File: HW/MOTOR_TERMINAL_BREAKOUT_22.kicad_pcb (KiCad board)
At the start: 2 copper layers, 20 x 28 mm, 12 parts

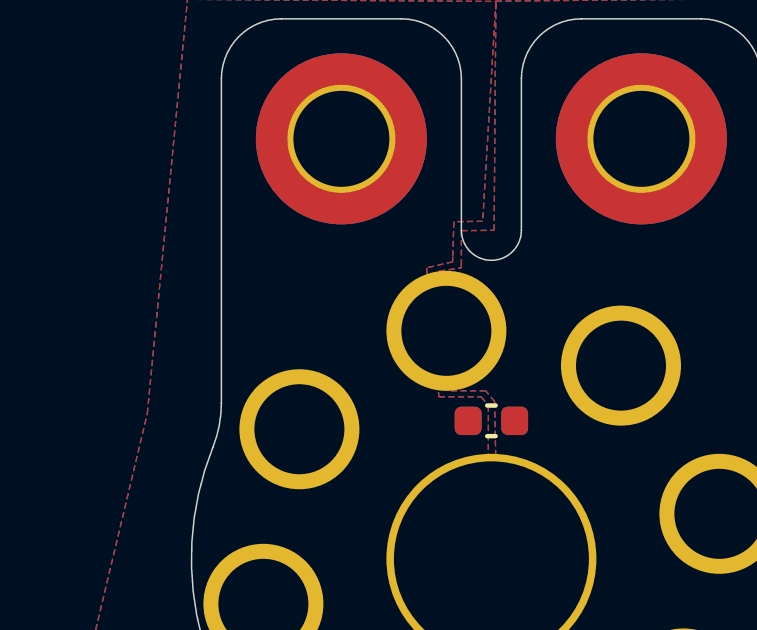
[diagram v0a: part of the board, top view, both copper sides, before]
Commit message: Update Silkscreen to Add Revision Number
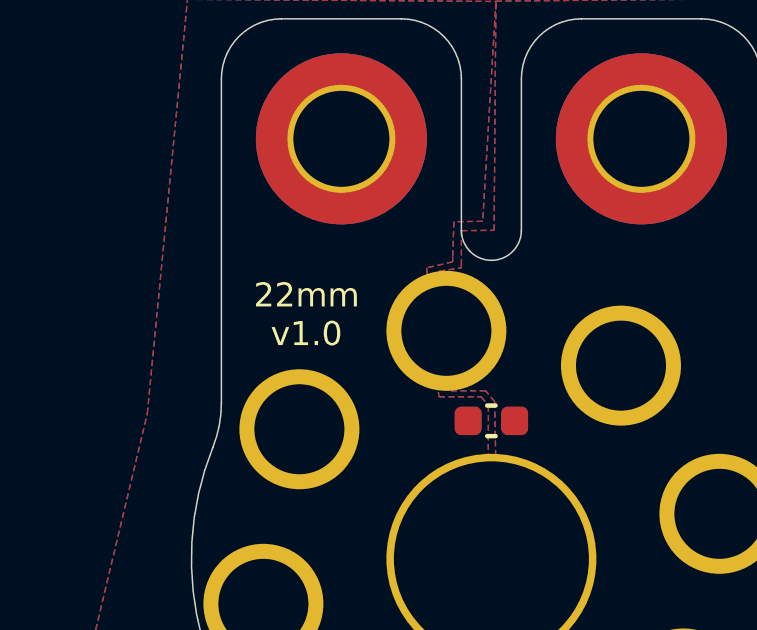
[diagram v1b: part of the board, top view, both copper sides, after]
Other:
- board text added: "22mm v1.0"
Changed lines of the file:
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@@
   (gr_line (start 221 134) (end 221 139.050126) (layer "Edge.Cuts") (width 0.05))
   (gr_arc (start 221 134) (mid 221.585786 132.585786) (end 223 132) (layer "Edge.Cuts") (width 0.05))
+  (gr_text "22mm\nv1.0" (at 213.84 141.86) (layer "F.SilkS")
+    (effects (font (size 0.8 0.8) (thickness 0.2)))
+  )
   (zone (net 2) (net_name "+BATT") (layers F&B.Cu) (hatch edge 0.508)
     (connect_pads yes (clearance 0.2))

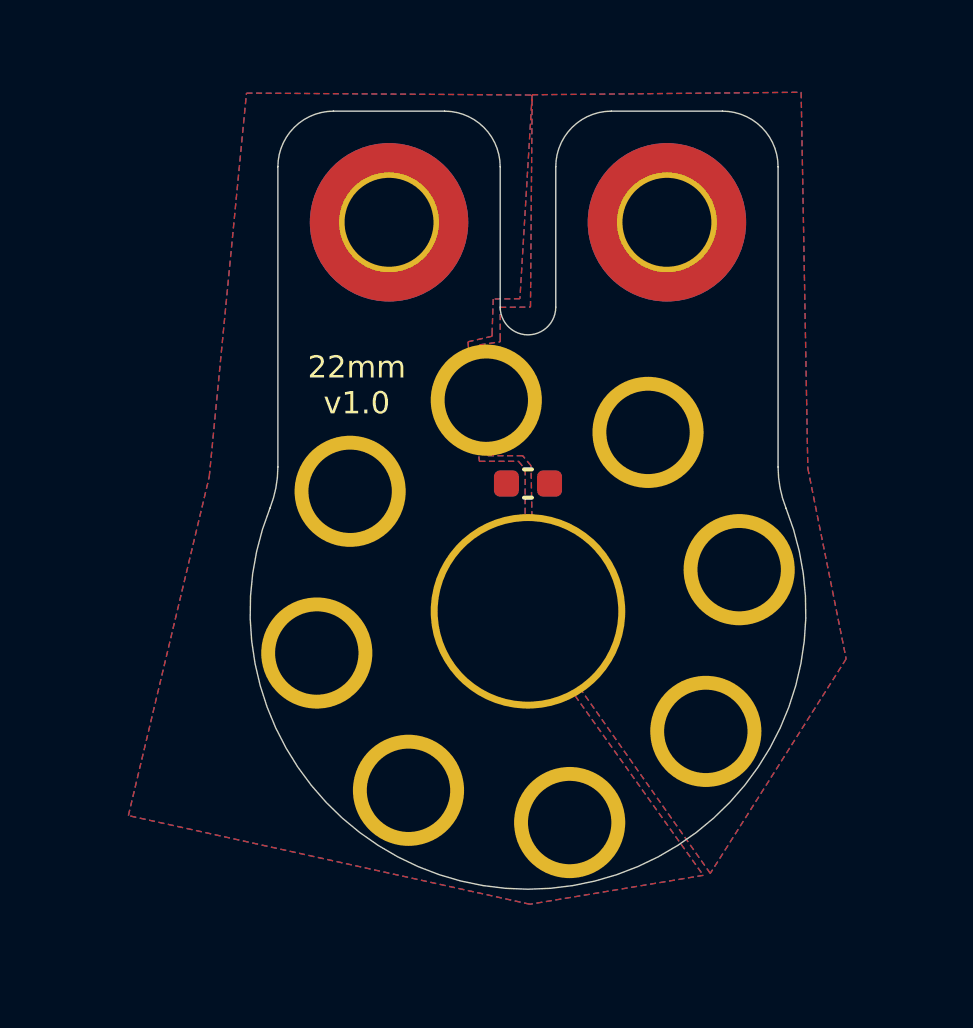
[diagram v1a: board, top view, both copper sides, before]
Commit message: Update design to v1.1 for next manufacturing run
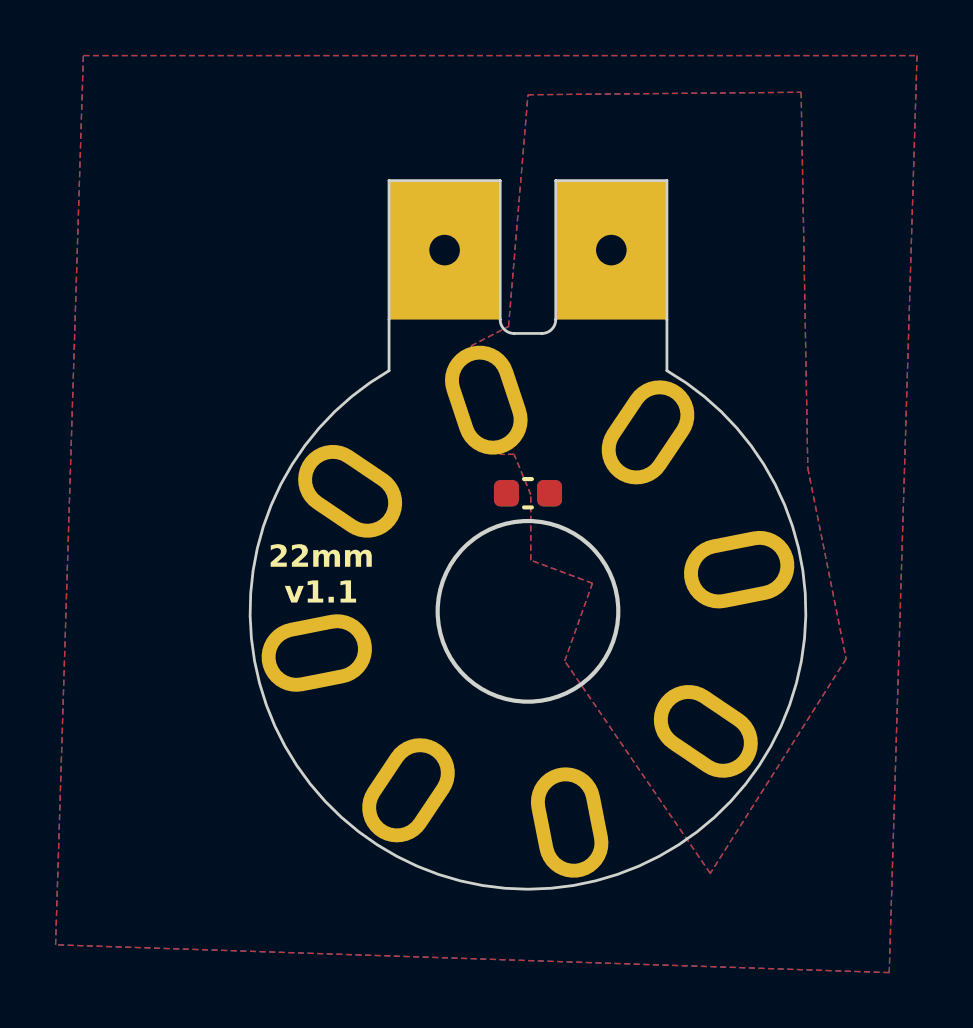
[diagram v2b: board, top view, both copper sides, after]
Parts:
- removed H1, H2: MountingHole_Pad, MountingHole:MountingHole_3.2mm_M3_ISO7380_Pad_TopBottom
- removed H10, H3, H4, H5, H6, H7, H8, H9: MountingHole_Pad, MountingHole:MountingHole_3mm_Pad_TopBottom
- removed H13: MountingHole_Pad, MountingHole:MountingHole_6.5mm
- added M1: 22 Motor Terminal Lead, MOTOR_TERMINAL_BREAKOUT:22 Motor Terminal Lead, F.Cu at (218.5, 142.4)
- added M2: 22 Motor Terminal Lead, MOTOR_TERMINAL_BREAKOUT:22 Motor Terminal Lead, F.Cu at (224.3, 143.6)
- added M3: 22 Motor Terminal Lead, MOTOR_TERMINAL_BREAKOUT:22 Motor Terminal Lead, F.Cu at (227.6, 148.5)
- added M4: 22 Motor Terminal Lead, MOTOR_TERMINAL_BREAKOUT:22 Motor Terminal Lead, F.Cu at (226.4, 154.3)
- added M5: 22 Motor Terminal Lead, MOTOR_TERMINAL_BREAKOUT:22 Motor Terminal Lead, F.Cu at (221.5, 157.6)
- added M6: 22 Motor Terminal Lead, MOTOR_TERMINAL_BREAKOUT:22 Motor Terminal Lead, F.Cu at (215.7, 156.4)
- added M7: 22 Motor Terminal Lead, MOTOR_TERMINAL_BREAKOUT:22 Motor Terminal Lead, F.Cu at (212.4, 151.5)
- added M8: 22 Motor Terminal Lead, MOTOR_TERMINAL_BREAKOUT:22 Motor Terminal Lead, F.Cu at (213.6, 145.7)
- added N1: Finger_4x5_M1, N_NonPart:Finger_4x5_M1, F.Cu at (223.0, 137.0)
- added N2: Finger_4x5_M1, N_NonPart:Finger_4x5_M1, F.Cu at (217.0, 137.0)
- C1: value C_0603 -> 10nF 50V
- moved C1 0.35 mm to (220.0, 145.8)
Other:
- board size 20 x 28 mm -> 20 x 20.5 mm
- board text added: "22mm v1.1"
- board text removed: "22mm v1.0"
